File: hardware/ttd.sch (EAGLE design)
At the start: 19 parts, among them Q1 IRFZ44N, Q2 IRFZ44N, Q3 IRFZ44N, Q4 IRFZ44N, X1 MKDSN1,5/2-5,08, X2 MKDSN1,5/2-5,08

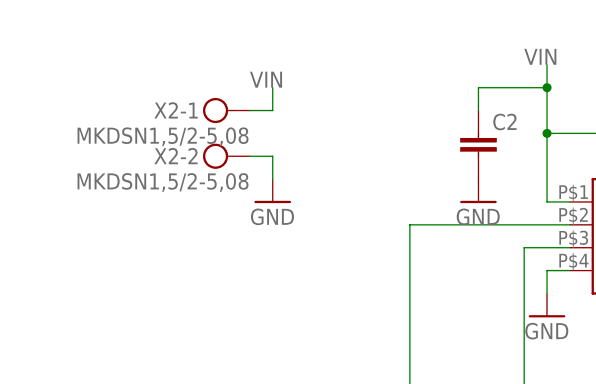
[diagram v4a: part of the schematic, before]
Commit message: Elektrolytkondensator eingefügt
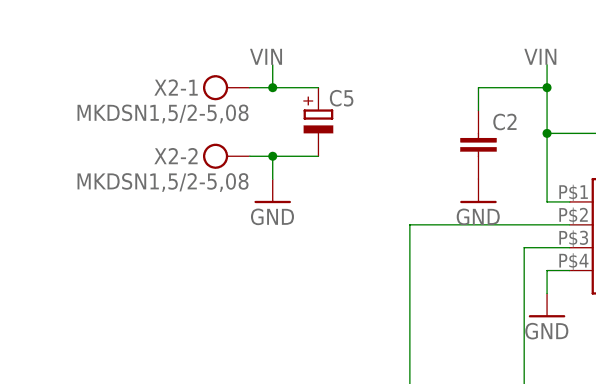
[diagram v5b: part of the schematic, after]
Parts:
- added C5: (no value), resistor:CPOL-EUE7.5-18
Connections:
- net GND: now also C5.-
- net VIN: now also C5.+
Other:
- moved on the sheet: X2-1
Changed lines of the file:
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@@
 <class number="0" name="Signal" width="0.254" drill="0">
 </class>
-<class number="1" name="Supply" width="1.27" drill="0">
+<class number="1" name="Supply" width="1.016" drill="0">
 </class>
 <class number="2" name="Motor" width="1.016" drill="0">
@@
 <part name="X3" library="con-phoenix-254" deviceset="MPT4" device=""/>
 <part name="GND8" library="supply1" deviceset="GND" device=""/>
+<part name="C5" library="resistor" deviceset="CPOL-EU" device="E7.5-18"/>
 </parts>
 <sheets>
@@
 <instance part="X1" gate="-1" x="121.92" y="60.96"/>
 <instance part="X1" gate="-2" x="121.92" y="55.88"/>
-<instance part="X2" gate="-1" x="7.62" y="88.9" rot="MR0"/>
+<instance part="X2" gate="-1" x="7.62" y="91.44" rot="MR0"/>
 <instance part="X2" gate="-2" x="7.62" y="83.82" rot="MR0"/>
 <instance part="GND7" gate="1" x="12.7" y="78.74"/>
@@
 <instance part="X3" gate="-4" x="7.62" y="25.4" rot="MR0"/>
 <instance part="GND8" gate="1" x="12.7" y="20.32"/>
+<instance part="C5" gate="G$1" x="17.78" y="88.9"/>
 </instances>
 <busses>
@@
 <wire x1="10.16" y1="83.82" x2="12.7" y2="83.82" width="0.1524" layer="91"/>
 <wire x1="12.7" y1="83.82" x2="12.7" y2="81.28" width="0.1524" layer="91"/>
+<pinref part="C5" gate="G$1" pin="-"/>
+<wire x1="12.7" y1="83.82" x2="17.78" y2="83.82" width="0.1524" layer="91"/>
+<junction x="12.7" y="83.82"/>
 </segment>
 <segment>
@@
 <segment>
 <pinref part="X2" gate="-1" pin="KL"/>
-<wire x1="10.16" y1="88.9" x2="12.7" y2="88.9" width="0.1524" layer="91"/>
-<wire x1="12.7" y1="88.9" x2="12.7" y2="91.44" width="0.1524" layer="91"/>
-<label x="10.16" y="91.44" size="1.778" layer="95"/>
+<wire x1="10.16" y1="91.44" x2="12.7" y2="91.44" width="0.1524" layer="91"/>
+<label x="10.16" y="93.98" size="1.778" layer="95"/>
+<wire x1="12.7" y1="91.44" x2="12.7" y2="93.98" width="0.1524" layer="91"/>
+<junction x="12.7" y="91.44"/>
+<pinref part="C5" gate="G$1" pin="+"/>
+<wire x1="12.7" y1="91.44" x2="17.78" y2="91.44" width="0.1524" layer="91"/>
 </segment>
 <segment>
@@
 </segment>
 </net>
-<net name="B" class="2">
+<net name="B" class="0">
 <segment>
 <pinref part="X3" gate="-2" pin="1"/>

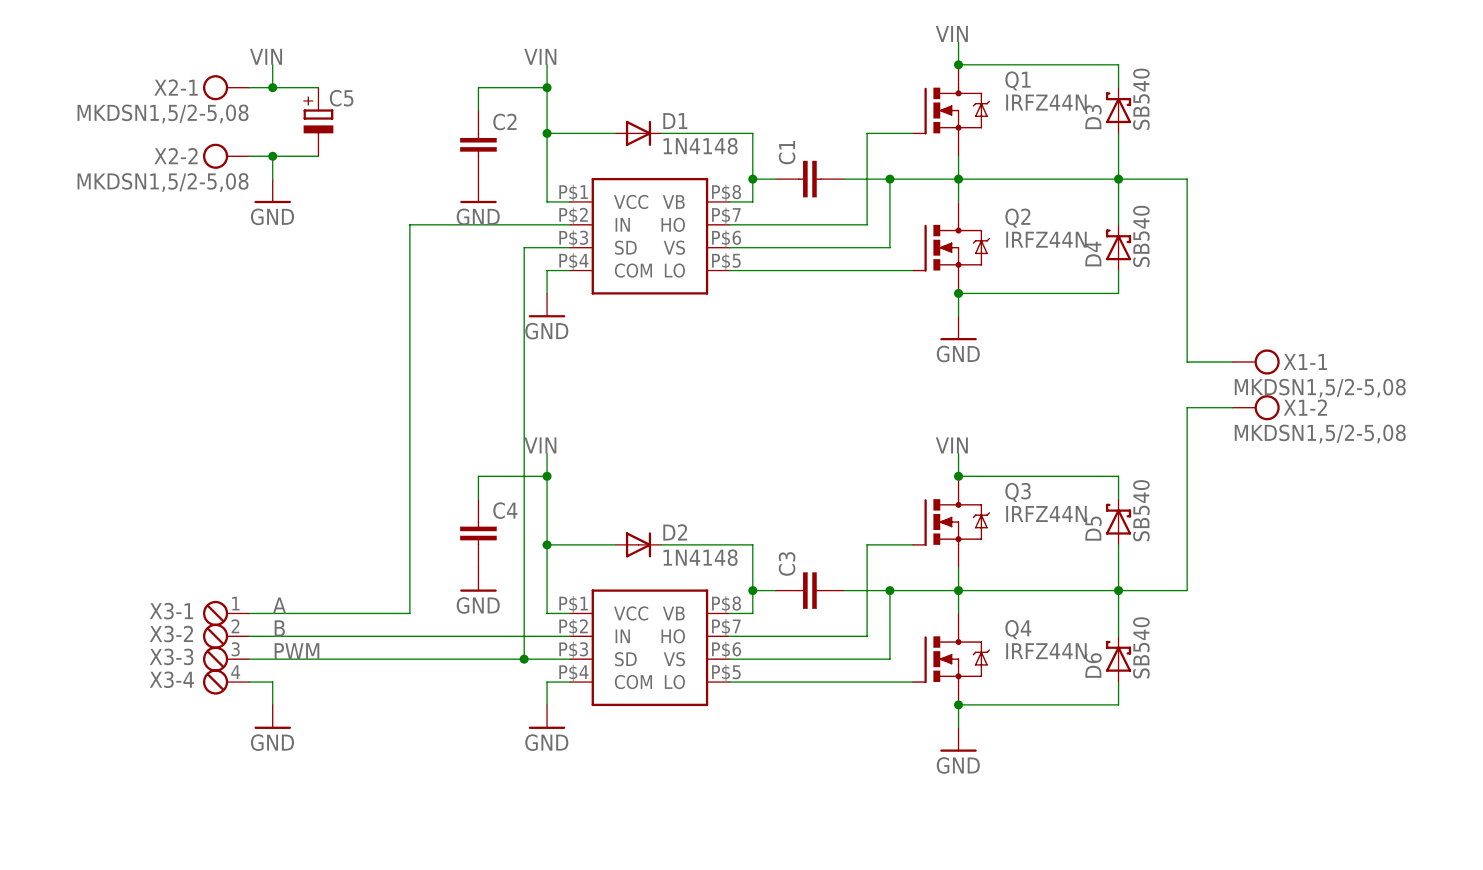
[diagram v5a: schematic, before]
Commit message: Änderungen beim Aufbau im Layout nachgetragen, Bauteilwerte eingetragen
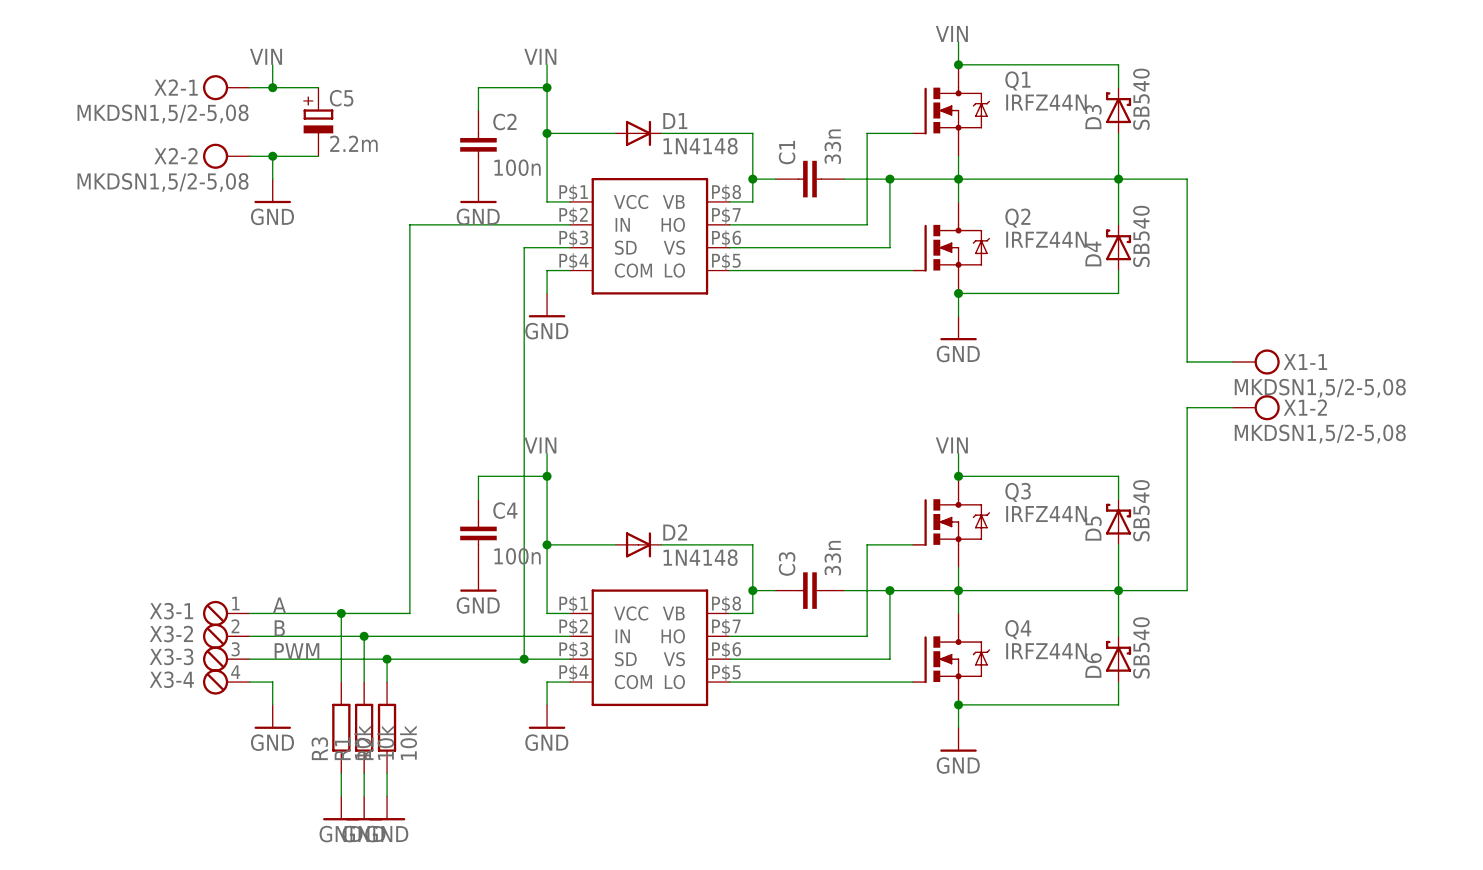
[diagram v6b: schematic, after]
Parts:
- added R1, R2: 10k, resistor:R-EU_0207/7
- added R3: 10k, resistor:R-EU_0207/10
- C1, C3: value (none) -> 33n
- C2, C4: value (none) -> 100n
- C5: value (none) -> 2.2m
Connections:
- net A: now also R3.2
- net B: now also R1.2
- net GND: now also R1.1, R2.1, R3.1
- net PWM: now also R2.2
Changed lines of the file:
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@@
 <part name="Q3" library="transistor-power" deviceset="IRF540" device="" value="IRFZ44N"/>
 <part name="Q4" library="transistor-power" deviceset="IRF540" device="" value="IRFZ44N"/>
-<part name="C1" library="rcl" deviceset="C-EU" device="050-025X075"/>
-<part name="C2" library="resistor" deviceset="C-EU" device="075-032X103"/>
-<part name="C3" library="rcl" deviceset="C-EU" device="050-025X075"/>
-<part name="C4" library="resistor" deviceset="C-EU" device="075-032X103"/>
+<part name="C1" library="rcl" deviceset="C-EU" device="050-025X075" value="33n"/>
+<part name="C2" library="resistor" deviceset="C-EU" device="075-032X103" value="100n"/>
+<part name="C3" library="rcl" deviceset="C-EU" device="050-025X075" value="33n"/>
+<part name="C4" library="resistor" deviceset="C-EU" device="075-032X103" value="100n"/>
 <part name="D1" library="diode" deviceset="1N4148" device="DO35-10" value="1N4148"/>
 <part name="D2" library="diode" deviceset="1N4148" device="DO35-10" value="1N4148"/>
@@
 <part name="X3" library="con-phoenix-254" deviceset="MPT4" device=""/>
 <part name="GND8" library="supply1" deviceset="GND" device=""/>
-<part name="C5" library="resistor" deviceset="CPOL-EU" device="E7.5-18"/>
+<part name="C5" library="resistor" deviceset="CPOL-EU" device="E7.5-18" value="2.2m"/>
+<part name="R1" library="resistor" deviceset="R-EU_" device="0207/7" value="10k"/>
+<part name="R2" library="resistor" deviceset="R-EU_" device="0207/7" value="10k"/>
+<part name="R3" library="resistor" deviceset="R-EU_" device="0207/10" value="10k"/>
+<part name="GND9" library="supply1" deviceset="GND" device=""/>
+<part name="GND10" library="supply1" deviceset="GND" device=""/>
+<part name="GND11" library="supply1" deviceset="GND" device=""/>
 </parts>
 <sheets>
@@
 <instance part="GND8" gate="1" x="12.7" y="20.32"/>
 <instance part="C5" gate="G$1" x="17.78" y="88.9"/>
+<instance part="R1" gate="G$1" x="22.86" y="20.32" rot="R90"/>
+<instance part="R2" gate="G$1" x="25.4" y="20.32" rot="R90"/>
+<instance part="R3" gate="G$1" x="20.32" y="20.32" rot="R90"/>
+<instance part="GND9" gate="1" x="20.32" y="10.16"/>
+<instance part="GND10" gate="1" x="22.86" y="10.16"/>
+<instance part="GND11" gate="1" x="25.4" y="10.16"/>
 </instances>
 <busses>
@@
 <wire x1="12.7" y1="25.4" x2="12.7" y2="22.86" width="0.1524" layer="91"/>
 </segment>
+<segment>
+<pinref part="GND9" gate="1" pin="GND"/>
+<pinref part="R3" gate="G$1" pin="1"/>
+<wire x1="20.32" y1="12.7" x2="20.32" y2="15.24" width="0.1524" layer="91"/>
+</segment>
+<segment>
+<pinref part="GND10" gate="1" pin="GND"/>
+<pinref part="R1" gate="G$1" pin="1"/>
+<wire x1="22.86" y1="12.7" x2="22.86" y2="15.24" width="0.1524" layer="91"/>
+</segment>
+<segment>
+<pinref part="R2" gate="G$1" pin="1"/>
+<pinref part="GND11" gate="1" pin="GND"/>
+<wire x1="25.4" y1="15.24" x2="25.4" y2="12.7" width="0.1524" layer="91"/>
+</segment>
 </net>
 <net name="PWM" class="0">
@@
 <pinref part="U$2" gate="G$1" pin="SD"/>
 <wire x1="40.64" y1="27.94" x2="45.72" y2="27.94" width="0.1524" layer="91"/>
-<wire x1="40.64" y1="27.94" x2="10.16" y2="27.94" width="0.1524" layer="91"/>
+<wire x1="40.64" y1="27.94" x2="25.4" y2="27.94" width="0.1524" layer="91"/>
 <junction x="40.64" y="27.94"/>
 <pinref part="X3" gate="-3" pin="1"/>
 <label x="12.7" y="27.94" size="1.778" layer="95"/>
+<pinref part="R2" gate="G$1" pin="2"/>
+<wire x1="25.4" y1="27.94" x2="10.16" y2="27.94" width="0.1524" layer="91"/>
+<wire x1="25.4" y1="25.4" x2="25.4" y2="27.94" width="0.1524" layer="91"/>
+<junction x="25.4" y="27.94"/>
 </segment>
 </net>
@@
 <wire x1="45.72" y1="76.2" x2="27.94" y2="76.2" width="0.1524" layer="91"/>
 <wire x1="27.94" y1="76.2" x2="27.94" y2="33.02" width="0.1524" layer="91"/>
-<wire x1="27.94" y1="33.02" x2="10.16" y2="33.02" width="0.1524" layer="91"/>
+<wire x1="27.94" y1="33.02" x2="20.32" y2="33.02" width="0.1524" layer="91"/>
 <pinref part="X3" gate="-1" pin="1"/>
 <label x="12.7" y="33.02" size="1.778" layer="95"/>
+<pinref part="R3" gate="G$1" pin="2"/>
+<wire x1="20.32" y1="33.02" x2="10.16" y2="33.02" width="0.1524" layer="91"/>
+<wire x1="20.32" y1="25.4" x2="20.32" y2="33.02" width="0.1524" layer="91"/>
+<junction x="20.32" y="33.02"/>
 </segment>
 </net>
@@
 <pinref part="X3" gate="-2" pin="1"/>
 <pinref part="U$2" gate="G$1" pin="IN"/>
-<wire x1="10.16" y1="30.48" x2="45.72" y2="30.48" width="0.1524" layer="91"/>
+<wire x1="10.16" y1="30.48" x2="22.86" y2="30.48" width="0.1524" layer="91"/>
 <label x="12.7" y="30.48" size="1.778" layer="95"/>
-</segment>
-</net>
+<pinref part="R1" gate="G$1" pin="2"/>
+<wire x1="22.86" y1="30.48" x2="45.72" y2="30.48" width="0.1524" layer="91"/>
+<wire x1="22.86" y1="30.48" x2="22.86" y2="25.4" width="0.1524" layer="91"/>
+<junction x="22.86" y="30.48"/>
+</segment>
+</net>
